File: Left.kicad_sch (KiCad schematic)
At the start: 27 parts, among them J3 USB_B_Micro, J4 Conn_01x02, U4 NCP1117-3.3_SOT223, U5 W25Q128JVS, U6 RP2040, Y2 ABLS-12.000MHZ-B4-T

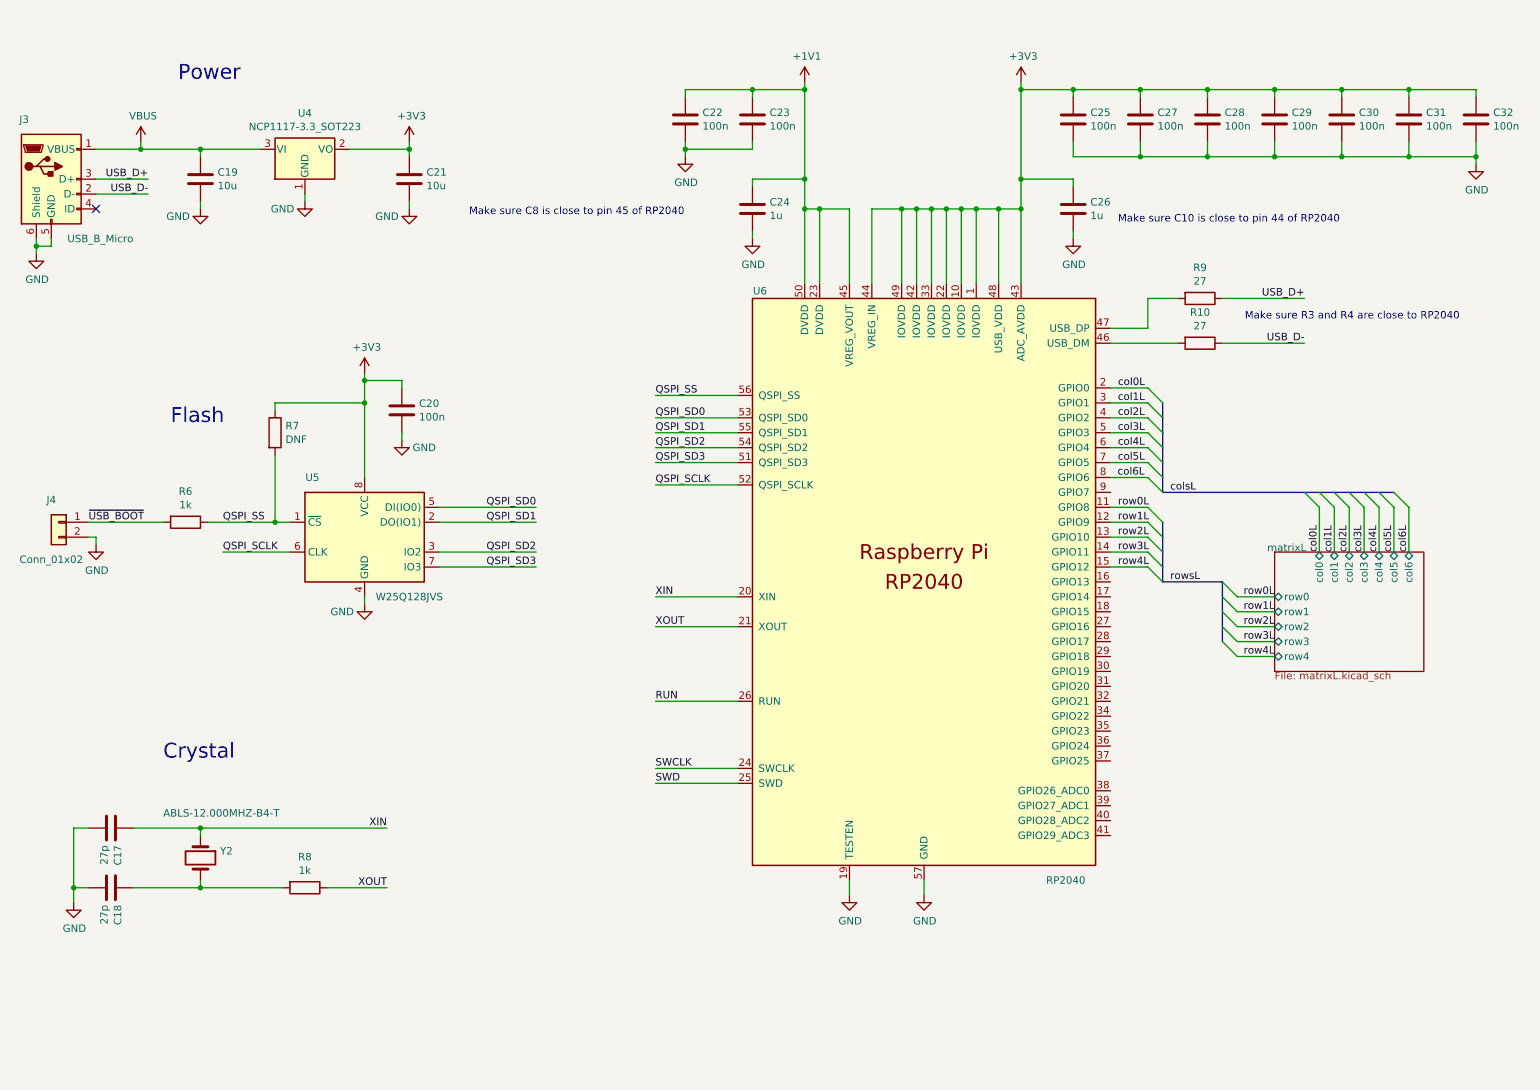
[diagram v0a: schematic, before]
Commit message: Hot pluggable trrs
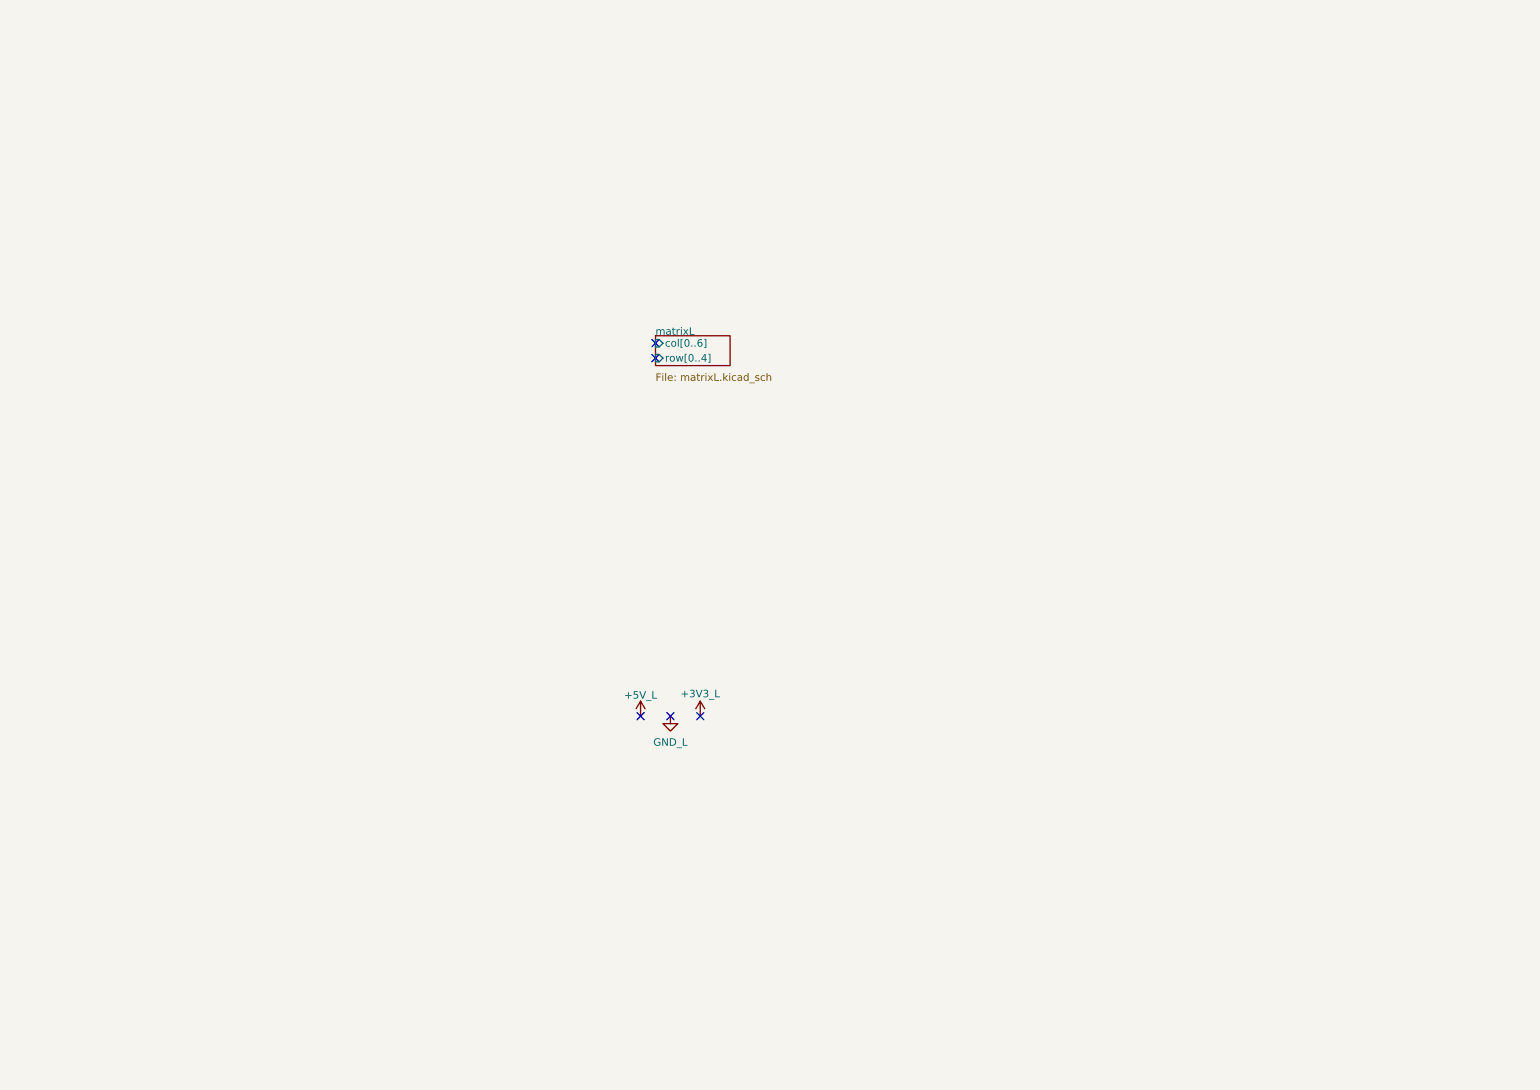
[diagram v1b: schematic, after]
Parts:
- removed C17, C18: 27p, Capacitor_SMD:C_0402_1005Metric, symbol Device:C
- removed C19, C21: 10u, Capacitor_SMD:C_0805_2012Metric, symbol Device:C
- removed C20, C22, C23, C25, C27, C28, C29, C30, C31, C32: 100n, Capacitor_SMD:C_0402_1005Metric, symbol Device:C
- removed C24, C26: 1u, Capacitor_SMD:C_0402_1005Metric, symbol Device:C
- removed J3: USB_B_Micro, RP2040_minimal:USB_Micro-B_Amphenol_10103594-0001LF_Horizontal_modified, symbol RP2040_minimal-rescue:USB_B_Micro-Connector
- removed J4: Conn_01x02, Connector_PinHeader_2.54mm:PinHeader_1x02_P2.54mm_Vertical, symbol Connector_Generic:Conn_01x02
- removed R10, R9: 27, Capacitor_SMD:C_0402_1005Metric, symbol Device:R
- removed R6, R8: 1k, Capacitor_SMD:C_0402_1005Metric, symbol Device:R
- removed R7: DNF, Capacitor_SMD:C_0402_1005Metric, symbol Device:R
- removed U4: NCP1117-3.3_SOT223, Package_TO_SOT_SMD:SOT-223-3_TabPin2, symbol Regulator_Linear:NCP1117-3.3_SOT223
- removed U5: W25Q128JVS, Package_SO:SOIC-8_5.23x5.23mm_P1.27mm, symbol Memory_Flash:W25Q128JVS
- removed U6: RP2040, RP2040_minimal:RP2040-QFN-56, symbol MCU_RaspberryPi_RP2040:RP2040
- removed Y2: ABLS-12.000MHZ-B4-T, RP2040_minimal:Crystal_SMD_HC49-US, symbol Device:Crystal
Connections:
- no-connect marks 1 -> 5
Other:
- sheet matrixL ports: added col[0..6], row[0..4]; removed col0, col1, col2, col3, col4, col5, col6, row0, row1, row2, row3, row4
- note removed: "Crystal"
- note removed: "Flash"
- note removed: "Make sure C10 is close to pin 44 of RP2040"
- note removed: "Make sure C8 is close to pin 45 of RP2040"
- note removed: "Make sure R3 and R4 are close to RP2040"
- note removed: "Power"

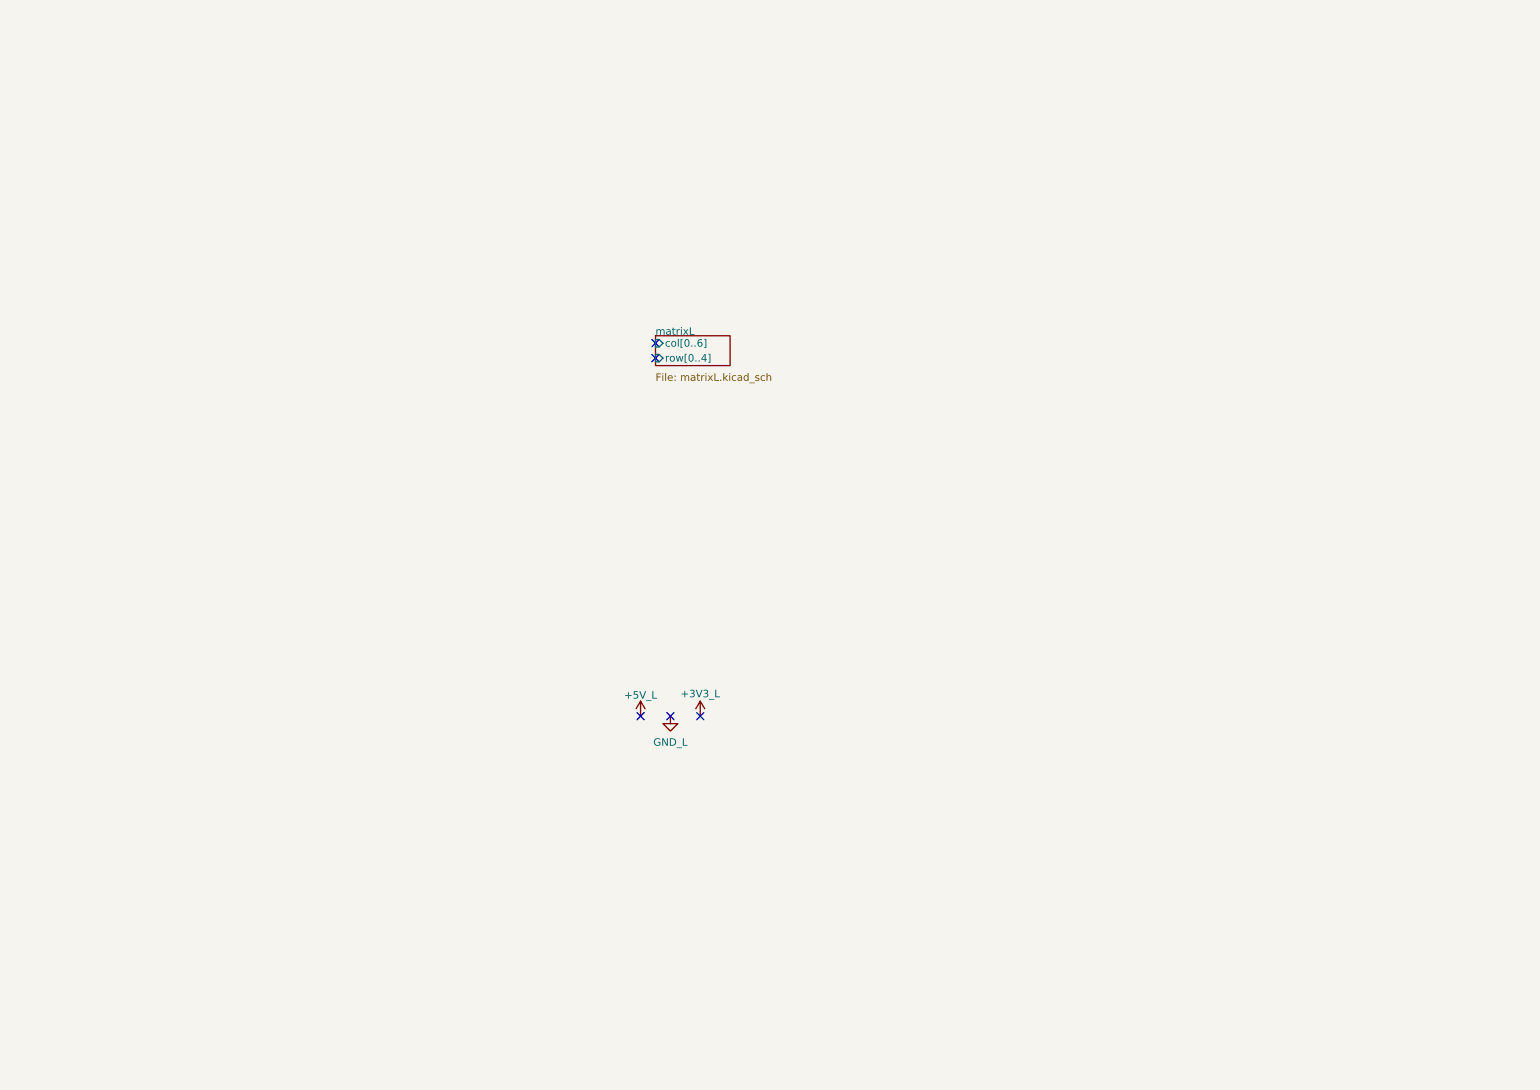
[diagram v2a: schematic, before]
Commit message: Add second micro back in, and added some footprints
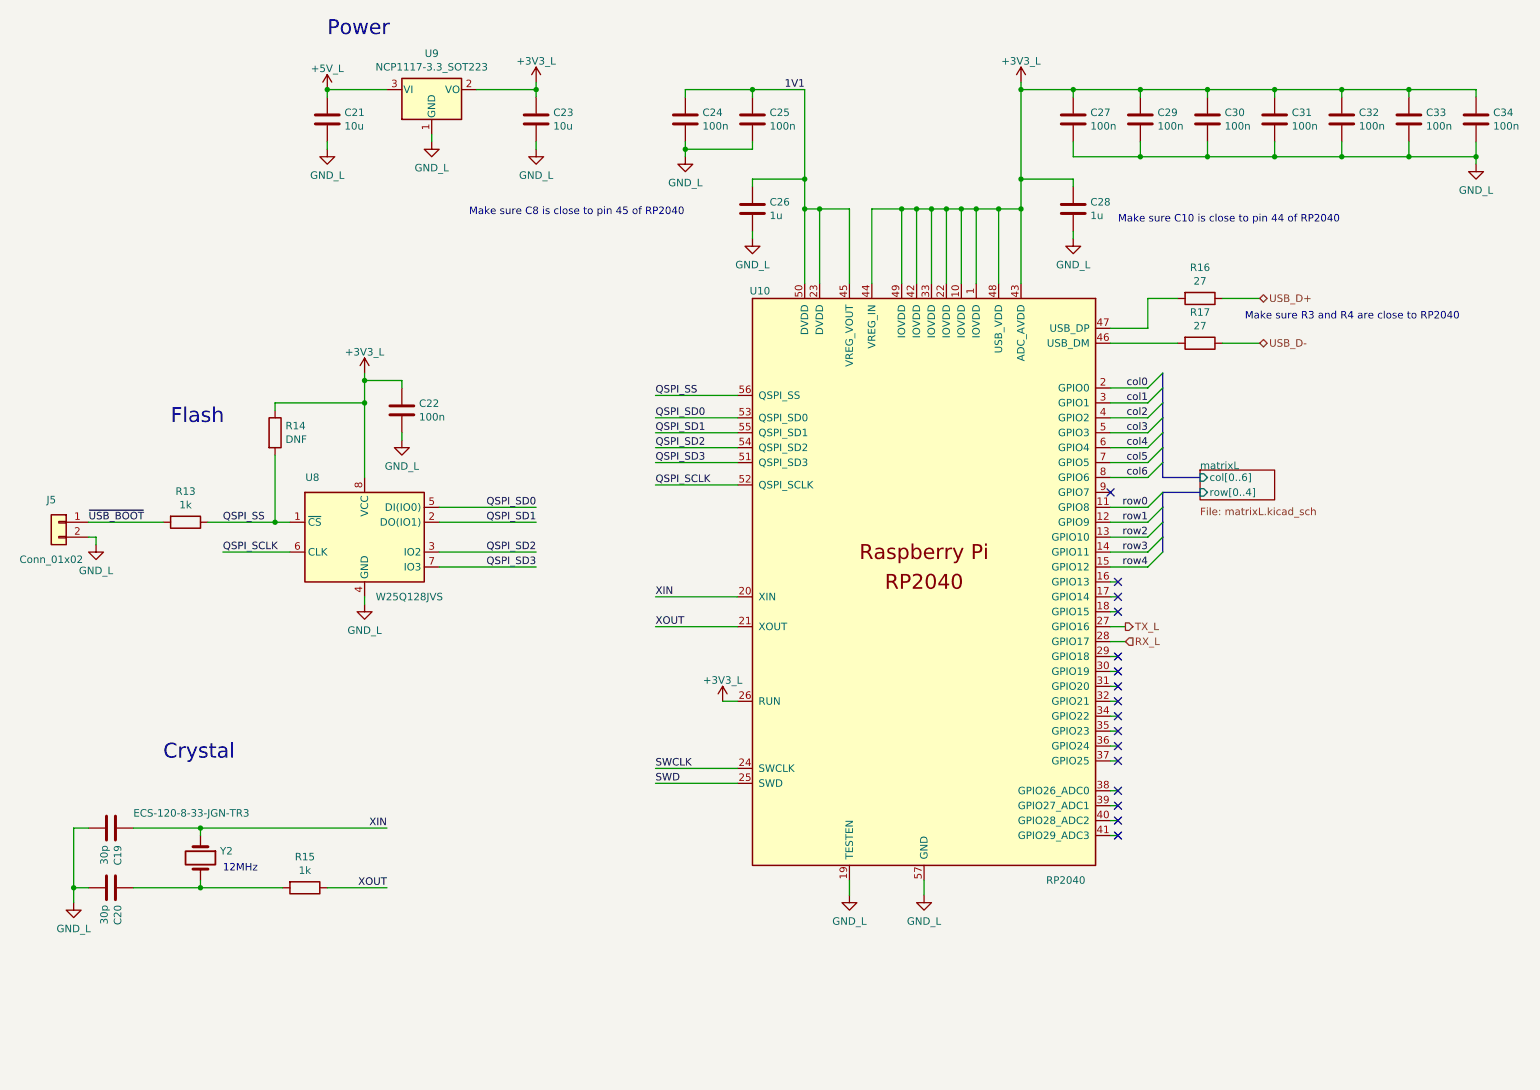
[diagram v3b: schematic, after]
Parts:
- added C19, C20: 30p, Capacitor_SMD:C_0402_1005Metric, symbol Device:C
- added C21, C23: 10u, Capacitor_SMD:C_0805_2012Metric, symbol Device:C
- added C22, C24, C25, C27, C29, C30, C31, C32, C33, C34: 100n, Capacitor_SMD:C_0402_1005Metric, symbol Device:C
- added C26, C28: 1u, Capacitor_SMD:C_0402_1005Metric, symbol Device:C
- added J5: Conn_01x02, Connector_PinHeader_2.54mm:PinHeader_1x02_P2.54mm_Vertical, symbol Connector_Generic:Conn_01x02
- added R13, R15: 1k, Capacitor_SMD:C_0402_1005Metric, symbol Device:R
- added R14: DNF, Capacitor_SMD:C_0402_1005Metric, symbol Device:R
- added R16, R17: 27, Capacitor_SMD:C_0402_1005Metric, symbol Device:R
- added U10: RP2040, RP2040_minimal:RP2040-QFN-56, symbol MCU_RaspberryPi_RP2040:RP2040
- added U8: W25Q128JVS, Package_SO:SOIC-8_5.23x5.23mm_P1.27mm, symbol Memory_Flash:W25Q128JVS
- added U9: NCP1117-3.3_SOT223, Package_TO_SOT_SMD:SOT-223-3_TabPin2, symbol Regulator_Linear:NCP1117-3.3_SOT223
- added Y2: ECS-120-8-33-JGN-TR3, Crystal:Crystal_SMD_EuroQuartz_MT-4Pin_3.2x2.5mm, symbol Device:Crystal
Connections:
- net +3V3_L: now also C22.1, C23.1, C27.1, C28.1, C29.1, C30.1, C31.1, C32.1, C33.1, C34.1, R14.1, U10.1 (IOVDD), U10.10 (IOVDD), U10.22 (IOVDD), U10.26 (RUN), U10.33 (IOVDD), U10.42 (IOVDD), U10.43 (ADC_AVDD), U10.44 (VREG_IN), U10.48 (USB_VDD), U10.49 (IOVDD), U8.8 (VCC), U9.2 (VO)
- net +5V_L: now also C21.1, U9.3 (VI)
- net GND_L: now also C19.2, C20.2, C21.2, C22.2, C23.2, C24.2, C25.2, C26.2, C27.2, C28.2, C29.2, C30.2, C31.2, C32.2, C33.2, C34.2, J5.2 (Pin_2), U10.19 (TESTEN), U10.57 (GND), U8.4 (GND), U9.1 (GND)
- new net: C20.1, R15.2, Y2.2
- new net: R17.2, U10.46 (USB_DM)
- new net: R16.2, U10.47 (USB_DP)
- new net 1V1: C24.1, C25.1, C26.1, U10.23 (DVDD), U10.45 (VREG_VOUT), U10.50 (DVDD)
- new net QSPI_SCLK: U10.52 (QSPI_SCLK), U8.6 (CLK)
- new net QSPI_SD0: U10.53 (QSPI_SD0), U8.5 (DI(IO0))
- new net QSPI_SD1: U10.55 (QSPI_SD1), U8.2 (DO(IO1))
- new net QSPI_SD2: U10.54 (QSPI_SD2), U8.3 (IO2)
- new net QSPI_SD3: U10.51 (QSPI_SD3), U8.7 (IO3)
- new net QSPI_SS: R13.1, R14.2, U10.56 (QSPI_SS), U8.1 (~{CS})
- new net RX_L: U10.28 (GPIO17)
- new net SWCLK: U10.24 (SWCLK)
- new net SWD: U10.25 (SWD)
- new net TX_L: U10.27 (GPIO16)
- new net USB_D+: R16.1
- new net USB_D-: R17.1
- new net XIN: C19.1, U10.20 (XIN), Y2.1
- new net XOUT: R15.1, U10.21 (XOUT)
- new net col0: U10.2 (GPIO0)
- new net col1: U10.3 (GPIO1)
- new net col2: U10.4 (GPIO2)
- new net col3: U10.5 (GPIO3)
- new net col4: U10.6 (GPIO4)
- new net col5: U10.7 (GPIO5)
- new net col6: U10.8 (GPIO6)
- new net row0: U10.11 (GPIO8)
- new net row1: U10.12 (GPIO9)
- new net row2: U10.13 (GPIO10)
- new net row3: U10.14 (GPIO11)
- new net row4: U10.15 (GPIO12)
- new net ~{USB_BOOT}: J5.1 (Pin_1), R13.2
- no-connect marks 5 -> 16
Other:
- note added: "12MHz"
- note added: "Crystal"
- note added: "Flash"
- note added: "Make sure C10 is close to pin 44 of RP2040"
- note added: "Make sure C8 is close to pin 45 of RP2040"
- note added: "Make sure R3 and R4 are close to RP2040"
- note added: "Power"

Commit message: Schematic mostly finished
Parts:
- Y2: symbol Device:Crystal -> Device:Crystal_GND24
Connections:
- net GND_L: now also Y2.2, Y2.4
- net at C20.1, R15.2: now also Y2.3; no longer Y2.2
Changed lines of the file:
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@@
     (effects (font (size 2.54 2.54)) (justify left bottom))
   )
-  (text "12MHz\n" (at 49.53 161.29 0)
+  (text "12MHz\n" (at 49.53 156.21 0)
     (effects (font (size 1.27 1.27)) (justify left bottom))
   )
@@
     )
     (property "Datasheet" "" (id 3) (at 85.09 36.83 0)
+      (effects (font (size 1.27 1.27)) hide)
+    )
+    (pin "1")
+  )
+  (symbol (lib_id "arisu-split:GND_L") (at 50.8 158.75 0) (unit 1)
+    (in_bom yes) (on_board yes)
+    (property "Reference" "#PWR0120" (id 0) (at 50.8 165.1 0)
+      (effects (font (size 1.27 1.27)) hide)
+    )
+    (property "Value" "GND_L" (id 1) (at 50.8 162.56 0))
+    (property "Footprint" "" (id 2) (at 50.8 158.75 0)
+      (effects (font (size 1.27 1.27)) hide)
+    )
+    (property "Datasheet" "" (id 3) (at 50.8 158.75 0)
       (effects (font (size 1.27 1.27)) hide)
     )
@@
     (pin "2")
   )
-  (symbol (lib_id "Device:Crystal") (at 45.72 158.75 270) (unit 1)
-    (in_bom yes) (on_board yes)
-    (property "Reference" "Y2" (id 0) (at 49.0474 157.5816 90)
+  (symbol (lib_id "arisu-split:GND_L") (at 40.64 158.75 0) (unit 1)
+    (in_bom yes) (on_board yes)
+    (property "Reference" "#PWR0121" (id 0) (at 40.64 165.1 0)
+      (effects (font (size 1.27 1.27)) hide)
+    )
+    (property "Value" "GND_L" (id 1) (at 40.64 162.56 0))
+    (property "Footprint" "" (id 2) (at 40.64 158.75 0)
+      (effects (font (size 1.27 1.27)) hide)
+    )
+    (property "Datasheet" "" (id 3) (at 40.64 158.75 0)
+      (effects (font (size 1.27 1.27)) hide)
+    )
+    (pin "1")
+  )
+  (symbol (lib_id "Device:Crystal_GND24") (at 45.72 158.75 270) (unit 1)
+    (in_bom yes) (on_board yes)
+    (property "Reference" "Y2" (id 0) (at 44.45 148.59 90)
       (effects (font (size 1.27 1.27)) (justify left))
     )
@@
     (pin "1")
     (pin "2")
+    (pin "3")
+    (pin "4")
   )
   (symbol (lib_id "Regulator_Linear:NCP1117-3.3_SOT223") (at 85.09 27.94 0) (unit 1)

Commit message: more layout, and some 3d files
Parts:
- removed U9: NCP1117-3.3_SOT223, Package_TO_SOT_SMD:SOT-223-3_TabPin2, symbol Regulator_Linear:NCP1117-3.3_SOT223
- added C36: 10n, Capacitor_SMD:C_0603_1608Metric, symbol Device:C
- added U1: LM1117-3.3, Package_TO_SOT_SMD:SOT-223-3_TabPin2, symbol Regulator_Linear:LM1117-3.3
- C22, R13, R14, R16, R17: footprint Capacitor_SMD:C_0402_1005Metric -> Capacitor_SMD:C_0603_1608Metric
- U8: footprint Package_SO:SOIC-8_5.23x5.23mm_P1.27mm -> arisu-split:SOIC-8_5.23x5.23mm_P1.27mm
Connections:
- net +3V3_L: now also C36.1, U1.2 (VO)
- net +5V_L: now also U1.3 (VI)
- net GND_L: now also C36.2, U1.1 (GND)
- net col0: now also U10.5 (GPIO3); no longer U10.2 (GPIO0)
- net col1: now also U10.6 (GPIO4); no longer U10.3 (GPIO1)
- net col2: now also U10.7 (GPIO5); no longer U10.4 (GPIO2)
- net col3: now also U10.8 (GPIO6); no longer U10.5 (GPIO3)
- net col4: now also U10.11 (GPIO8); no longer U10.6 (GPIO4)
- net col5: now also U10.12 (GPIO9); no longer U10.7 (GPIO5)
- net col6: now also U10.13 (GPIO10); no longer U10.8 (GPIO6)
- net row0: now also U10.14 (GPIO11); no longer U10.11 (GPIO8)
- net row1: now also U10.15 (GPIO12); no longer U10.12 (GPIO9)
- net row2: now also U10.16 (GPIO13); no longer U10.13 (GPIO10)
- net row3: now also U10.17 (GPIO14); no longer U10.14 (GPIO11)
- net row4: now also U10.18 (GPIO15); no longer U10.15 (GPIO12)
